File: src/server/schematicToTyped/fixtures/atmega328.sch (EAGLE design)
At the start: 7 parts, among them U3 ATMEGA328, Y1 8MHz

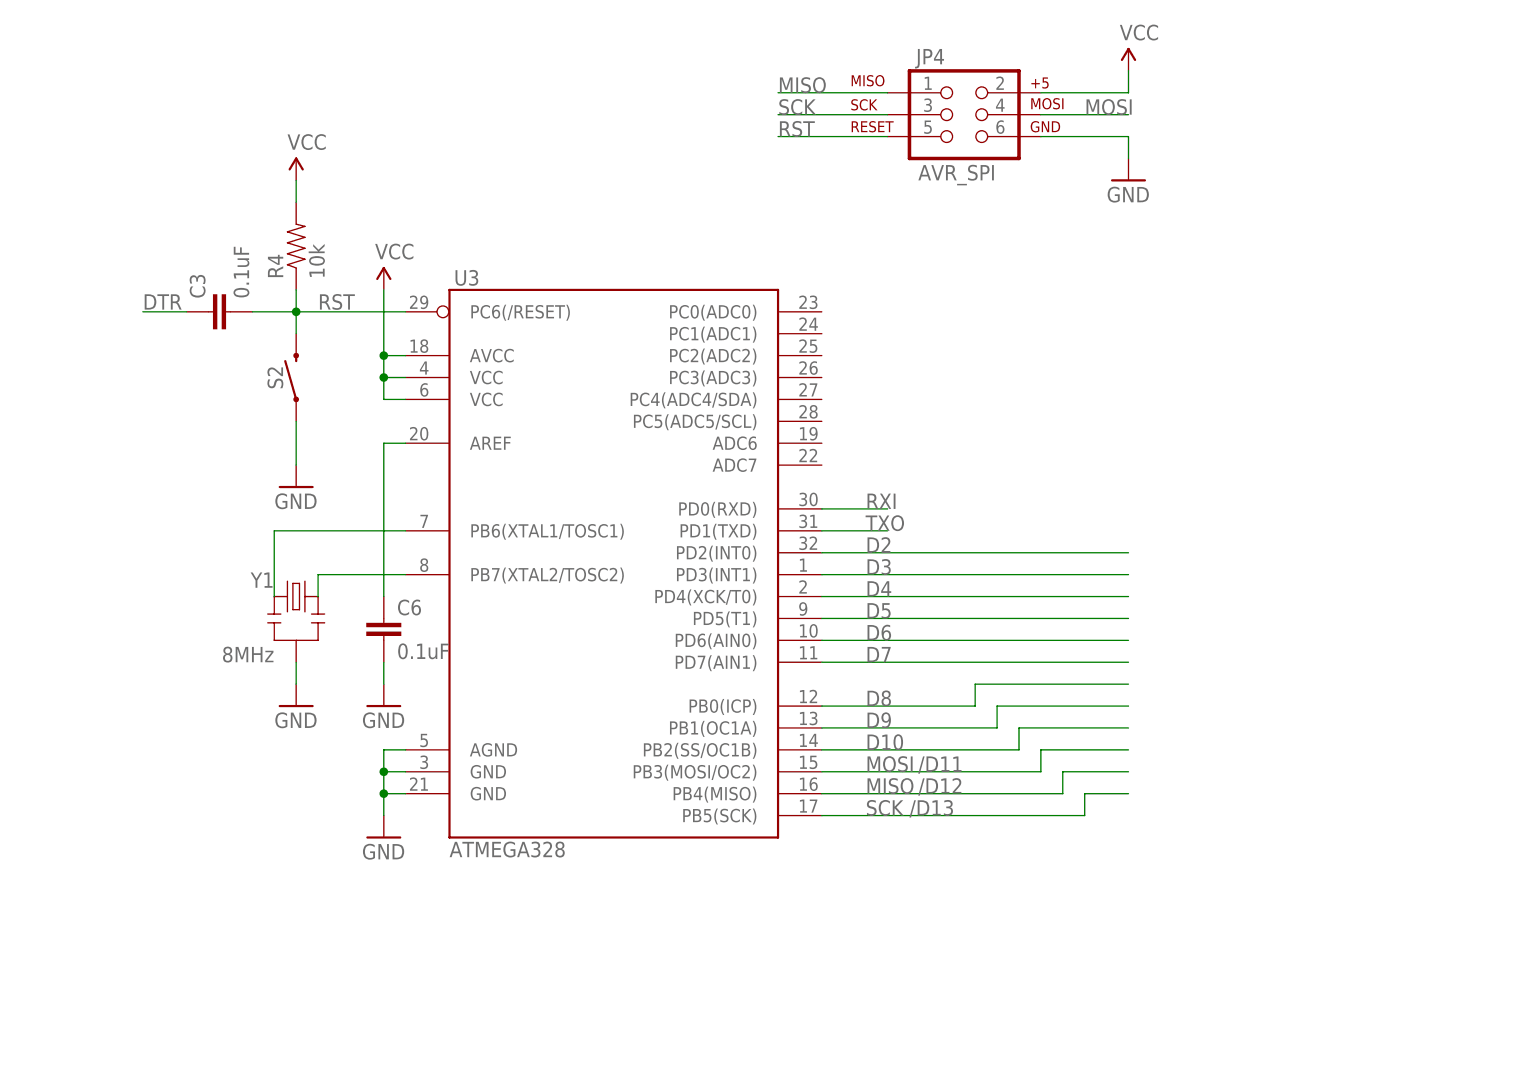
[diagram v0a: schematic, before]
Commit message: Adding Typed Atmega328
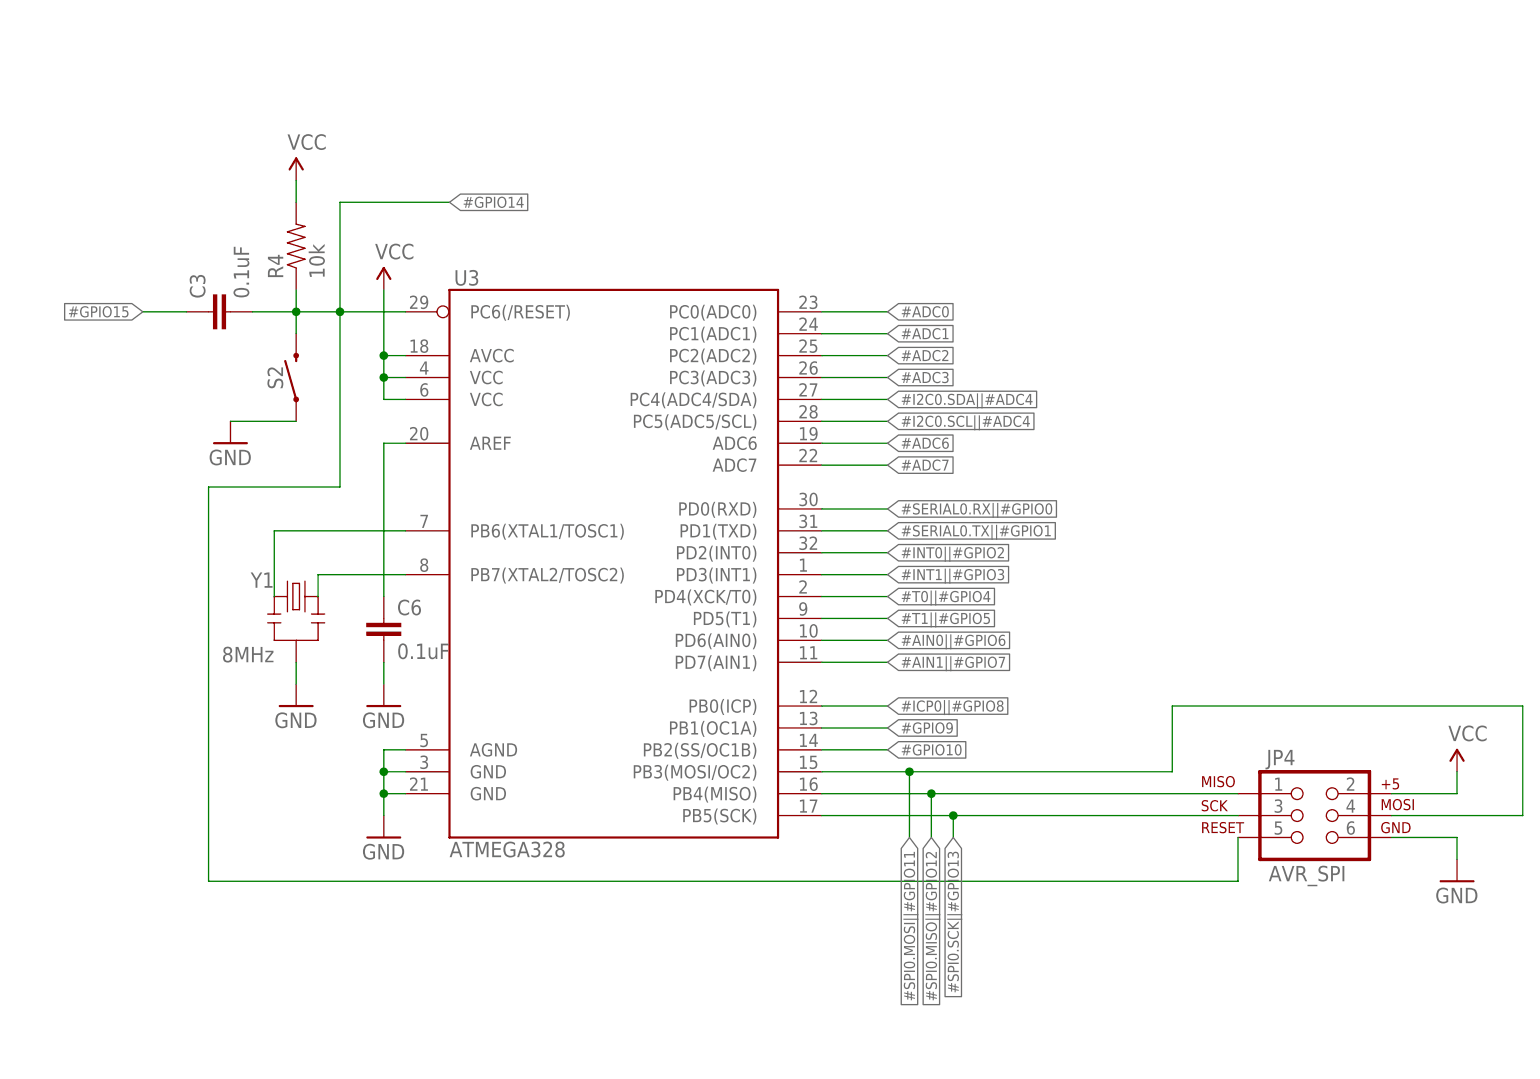
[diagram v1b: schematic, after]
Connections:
- net D10 renamed #GPIO10
- net D2 renamed #INT0||#GPIO2
- net D3 renamed #INT1||#GPIO3
- net D4 renamed #T0||#GPIO4
- net D5 renamed #T1||#GPIO5
- net D6 renamed #AIN0||#GPIO6
- net D7 renamed #AIN1||#GPIO7
- net D8 renamed #ICP0||#GPIO8
- net D9 renamed #GPIO9
- net DTR renamed #GPIO15
- net MISO renamed #SPI0.MISO||#GPIO12
- net MOSI renamed #SPI0.MOSI||#GPIO11
- net RST renamed #GPIO14
- net RXI renamed #SERIAL0.RX||#GPIO0
- net SCK renamed #SPI0.SCK||#GPIO13
- net TXO renamed #SERIAL0.TX||#GPIO1
- new net #ADC0: U3.PC0(ADC0)
- new net #ADC1: U3.PC1(ADC1)
- new net #ADC2: U3.PC2(ADC2)
- new net #ADC3: U3.PC3(ADC3)
- new net #ADC6: U3.ADC6
- new net #ADC7: U3.ADC7
- new net #I2C0.SCL||#ADC4: U3.PC5(ADC5/SCL)
- new net #I2C0.SDA||#ADC4: U3.PC4(ADC4/SDA)
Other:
- note removed: "/D11"
- note removed: "/D12"
- note removed: "/D13"
- moved on the sheet: JP4

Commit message: Improving typed schematics
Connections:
- net #GPIO14 renamed #GPIO-RESET
- net #GPIO15 renamed #GPIO-DTR
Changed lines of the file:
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@@
 </segment>
 </net>
-<net name="#GPIO14" class="0">
+<net name="#GPIO-RESET" class="0">
 <segment>
 <wire x1="63.5" y1="127" x2="63.5" y2="124.46" width="0.1524" layer="91"/>
@@
 </segment>
 </net>
-<net name="#GPIO15" class="0">
+<net name="#GPIO-DTR" class="0">
 <segment>
 <wire x1="50.8" y1="124.46" x2="45.72" y2="124.46" width="0.1524" layer="91"/>
